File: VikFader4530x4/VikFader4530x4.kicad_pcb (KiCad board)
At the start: 2 copper layers, 54.3 x 45.8 mm, 22 parts, among them J1 vik-module-connector, J3 Conn_01x04_Pin, U1 ADS1015IDGS

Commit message: Various DRC fixes
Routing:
- net GND: track 21.8 -> 28.0 mm, vias 1 -> 4
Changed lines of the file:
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@@
 		)
 		(pad "3" thru_hole circle
-			(at 21.75 -1.75 270)
-			(size 1.8 1.8)
-			(drill 1.2)
+			(at -17.6 4.25 270)
+			(size 2.55 2.55)
+			(drill 1.7)
 			(layers "*.Cu" "*.Mask")
 			(remove_unused_layers no)
 			(net 1 "GND")
-			(pintype "passive")
 			(solder_mask_margin 0.102)
 		)
-		(pad "SH1" thru_hole circle
+		(pad "3" thru_hole circle
 			(at -16.4 -4.25 270)
 			(size 2.55 2.55)
@@
 			(layers "*.Cu" "*.Mask")
 			(remove_unused_layers no)
+			(net 1 "GND")
 			(solder_mask_margin 0.102)
 		)
-		(pad "SH2" thru_hole circle
-			(at -17.6 4.25 270)
+		(pad "3" thru_hole circle
+			(at 16.4 -4.25 270)
 			(size 2.55 2.55)
 			(drill 1.7)
 			(layers "*.Cu" "*.Mask")
 			(remove_unused_layers no)
+			(net 1 "GND")
 			(solder_mask_margin 0.102)
 		)
-		(pad "SH3" thru_hole circle
-			(at 16.4 -4.25 270)
+		(pad "3" thru_hole circle
+			(at 17.6 4.25 270)
 			(size 2.55 2.55)
 			(drill 1.7)
 			(layers "*.Cu" "*.Mask")
 			(remove_unused_layers no)
+			(net 1 "GND")
 			(solder_mask_margin 0.102)
 		)
-		(pad "SH4" thru_hole circle
-			(at 17.6 4.25 270)
-			(size 2.55 2.55)
-			(drill 1.7)
+		(pad "3" thru_hole circle
+			(at 21.75 -1.75 270)
+			(size 1.8 1.8)
+			(drill 1.2)
 			(layers "*.Cu" "*.Mask")
 			(remove_unused_layers no)
+			(net 1 "GND")
+			(pintype "passive")
 			(solder_mask_margin 0.102)
 		)
@@
 		)
 		(pad "3" thru_hole circle
-			(at 21.75 -1.75 270)
-			(size 1.8 1.8)
-			(drill 1.2)
+			(at -17.6 4.25 270)
+			(size 2.55 2.55)
+			(drill 1.7)
 			(layers "*.Cu" "*.Mask")
 			(remove_unused_layers no)
 			(net 1 "GND")
-			(pintype "passive")
 			(solder_mask_margin 0.102)
 		)
-		(pad "SH1" thru_hole circle
+		(pad "3" thru_hole circle
 			(at -16.4 -4.25 270)
 			(size 2.55 2.55)
@@
 			(layers "*.Cu" "*.Mask")
 			(remove_unused_layers no)
+			(net 1 "GND")
 			(solder_mask_margin 0.102)
 		)
-		(pad "SH2" thru_hole circle
-			(at -17.6 4.25 270)
+		(pad "3" thru_hole circle
+			(at 16.4 -4.25 270)
 			(size 2.55 2.55)
 			(drill 1.7)
 			(layers "*.Cu" "*.Mask")
 			(remove_unused_layers no)
+			(net 1 "GND")
 			(solder_mask_margin 0.102)
 		)
-		(pad "SH3" thru_hole circle
-			(at 16.4 -4.25 270)
+		(pad "3" thru_hole circle
+			(at 17.6 4.25 270)
 			(size 2.55 2.55)
 			(drill 1.7)
 			(layers "*.Cu" "*.Mask")
 			(remove_unused_layers no)
+			(net 1 "GND")
 			(solder_mask_margin 0.102)
 		)
-		(pad "SH4" thru_hole circle
-			(at 17.6 4.25 270)
-			(size 2.55 2.55)
-			(drill 1.7)
+		(pad "3" thru_hole circle
+			(at 21.75 -1.75 270)
+			(size 1.8 1.8)
+			(drill 1.2)
 			(layers "*.Cu" "*.Mask")
 			(remove_unused_layers no)
+			(net 1 "GND")
+			(pintype "passive")
 			(solder_mask_margin 0.102)
 		)
@@
 	)
 	(via
+		(at 194.4 63.13)
+		(size 0.6)
+		(drill 0.3)
+		(layers "F.Cu" "B.Cu")
+		(net 1)
+	)
+	(via
 		(at 211.07 64.65)
 		(size 0.6)
@@
 		(net 1)
 	)
+	(via
+		(at 241.194515 48.505112)
+		(size 0.6)
+		(drill 0.3)
+		(layers "F.Cu" "B.Cu")
+		(net 1)
+	)
+	(via
+		(at 196.134328 48.382979)
+		(size 0.6)
+		(drill 0.3)
+		(layers "F.Cu" "B.Cu")
+		(net 1)
+	)
+	(segment
+		(start 194.9 63.63)
+		(end 194.4 63.13)
+		(width 0.2)
+		(layer "B.Cu")
+		(net 1)
+	)
+	(segment
+		(start 240.405 49.25)
+		(end 240.449627 49.25)
+		(width 0.2)
+		(layer "B.Cu")
+		(net 1)
+	)
 	(segment
 		(start 211.17 64.55)
@@
 	)
 	(segment
+		(start 195.407307 49.11)
+		(end 196.134328 48.382979)
+		(width 0.2)
+		(layer "B.Cu")
+		(net 1)
+	)
+	(segment
+		(start 194.9 64.9125)
+		(end 194.9 63.63)
+		(width 0.2)
+		(layer "B.Cu")
+		(net 1)
+	)
+	(segment
+		(start 193.9 63.63)
+		(end 194.4 63.13)
+		(width 0.2)
+		(layer "B.Cu")
+		(net 1)
+	)
+	(segment
 		(start 232.838 64.55)
 		(end 211.17 64.55)
 		(width 0.2)
 		(layer "B.Cu")
+		(net 1)
+	)
+	(segment
+		(start 195.36 49.11)
+		(end 195.407307 49.11)
+		(width 0.2)
+		(layer "B.Cu")
+		(net 1)
+	)
+	(segment
+		(start 240.449627 49.25)
+		(end 241.194515 48.505112)
+		(width 0.2)
+		(layer "B.Cu")
+		(net 1)
+	)
+	(segment
+		(start 193.9 64.9125)
+		(end 193.9 63.63)
+		(width 0.2)
+		(layer "B.Cu")

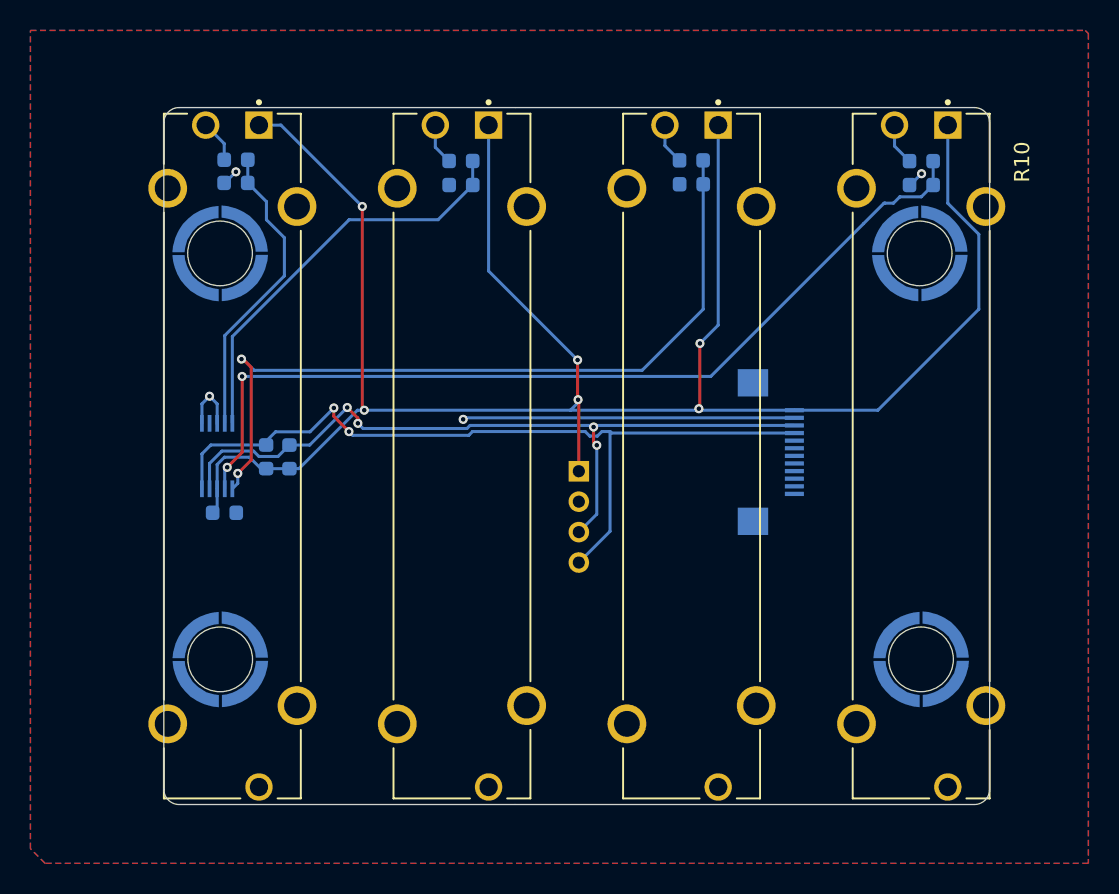
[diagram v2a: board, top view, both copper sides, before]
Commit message: All three models refactored to MOSFET setup
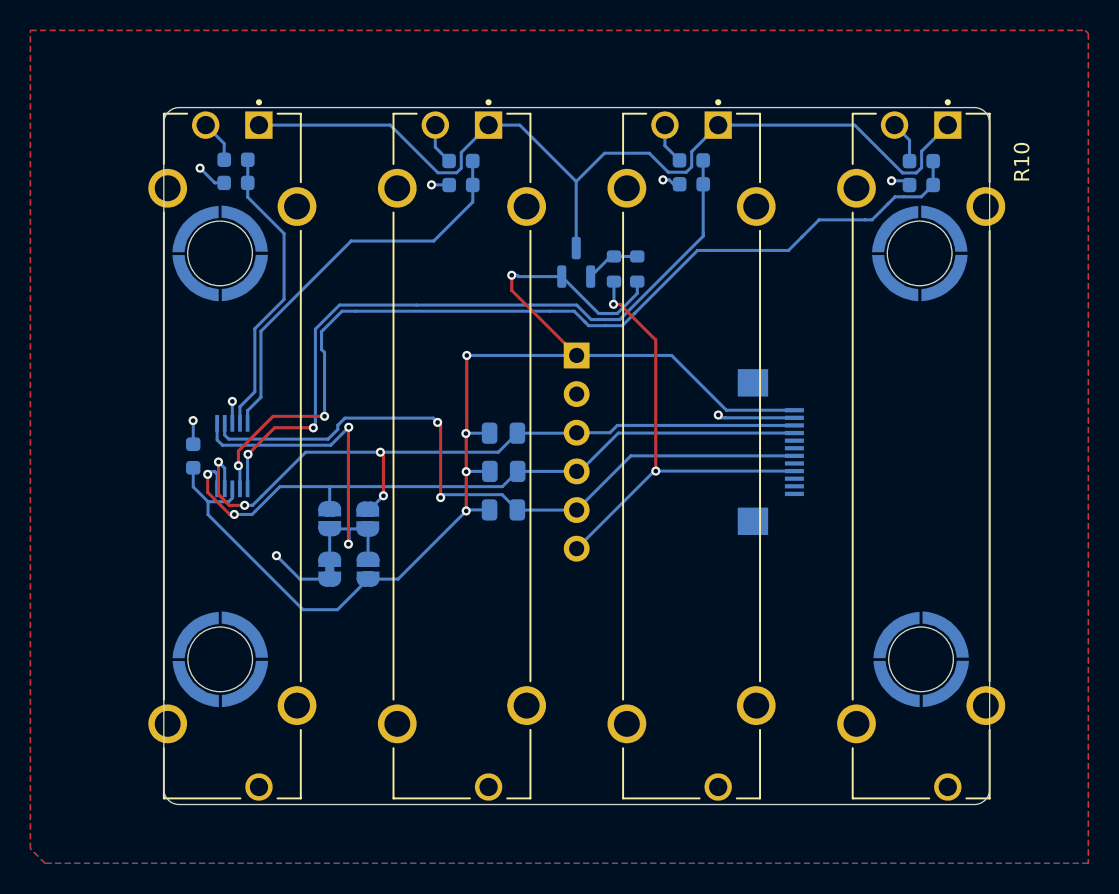
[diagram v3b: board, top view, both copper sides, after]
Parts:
- removed J3: Conn_01x04_Pin, Connector_PinHeader_2.00mm:PinHeader_1x04_P2.00mm_Vertical
- added J2: Conn_01x06_Pin, Connector_PinHeader_2.54mm:PinHeader_1x06_P2.54mm_Vertical, B.Cu at (218.5, 60.5)
- added JP1: 0x48, Jumper:SolderJumper-2_P1.3mm_Bridged_RoundedPad1.0x1.5mm, B.Cu at (202.3, 74.5)
- added JP2: 0x49, Jumper:SolderJumper-2_P1.3mm_Open_RoundedPad1.0x1.5mm, B.Cu at (204.8, 74.5)
- added JP3: 0x4A, Jumper:SolderJumper-2_P1.3mm_Open_RoundedPad1.0x1.5mm, B.Cu at (202.3, 71.2)
- added JP4: 0x4B, Jumper:SolderJumper-2_P1.3mm_Open_RoundedPad1.0x1.5mm, B.Cu at (204.8, 71.2)
- added Q1: DMG2305UX, Package_TO_SOT_SMD:SOT-23, B.Cu at (218.5, 54.3)
- added R11: 1kΩ, Resistor_SMD:R_0603_1608Metric, B.Cu at (221.0, 54.8)
- added R12: 100kΩ, Resistor_SMD:R_0603_1608Metric, B.Cu at (222.5, 54.8)
- added R13: 10kΩ, Resistor_SMD:R_0805_2012Metric, B.Cu at (213.7, 70.6)
- R2, R3: footprint Capacitor_SMD:C_0603_1608Metric -> Resistor_SMD:R_0805_2012Metric
- U1: value ADS1015IDGS -> ADS1115IDGS
- moved R3 15.6 mm to (213.7, 68.1), turned to 0 degrees
- moved R2 14.2 mm to (213.7, 65.6), turned to 0 degrees
- moved C2 4.26 mm to (193.3, 67.1), turned to 90 degrees
- moved U1 1.00 mm to (195.9, 67.1)
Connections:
- R1 pad 1: +3V3 -> FET-OUT
- R10 pad 1: +3V3 -> FET-OUT
- R5 pad 1: +3V3 -> FET-OUT
- R8 pad 1: +3V3 -> FET-OUT
- U1 pad 1: GND -> Net-(JP1-B)
- U1 pad 2: unconnected-(U1-ALERT/RDY-Pad2) -> GP1
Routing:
- net FET-OUT: track 0.00 -> 60.8 mm
- net +3V3: track 138.9 -> 83.7 mm, vias 6 -> 5
- net GP1: track 0.00 -> 46.0 mm, vias 0 -> 2
- net GP2: track 0.00 -> 30.3 mm, vias 0 -> 2
- net Net-(JP1-B): track 0.00 -> 25.6 mm, vias 0 -> 2
- net GND: track 28.0 -> 18.0 mm, vias 4 -> 8
- net SCL: track 53.5 -> 45.8 mm
- net POT-IN2: track 51.5 -> 47.6 mm
- net Net-(Q1-G): track 0.00 -> 3.61 mm
- net SDA: track 50.5 -> 48.7 mm
- net POT-IN3: track 60.1 -> 61.3 mm
- net POT-IN1: track 27.2 -> 26.6 mm
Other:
- board text added: "FET"
- board text added: "RDY"
